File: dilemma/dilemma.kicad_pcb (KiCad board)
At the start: 2 copper layers, 134 x 106.9 mm, 84 parts, among them J1 S3B-PH-SM4-TB(LF)(SN), J2 Serial, J3 BATTERY_CONN_DEANS, J5 S3B-PH-SM4-TB(LF)(SN), SW1 SW_Push, SW10 SW_Push, SW11 SW_Push, SW12 SW_Push, SW13 SW_Push, SW14 SW_Push, SW15 SW_Push, SW16 SW_Push, SW17 locked, SW18 SW_Push, SW2 SW_Push, SW26 SW_SPST, SW3 SW_Push, SW37 SW_SPST, SW4 SW_Push, SW5 SW_Push, SW6 SW_Push, SW7 SW_Push, SW8 SW_Push, SW9 SW_Push, U2 eliteC

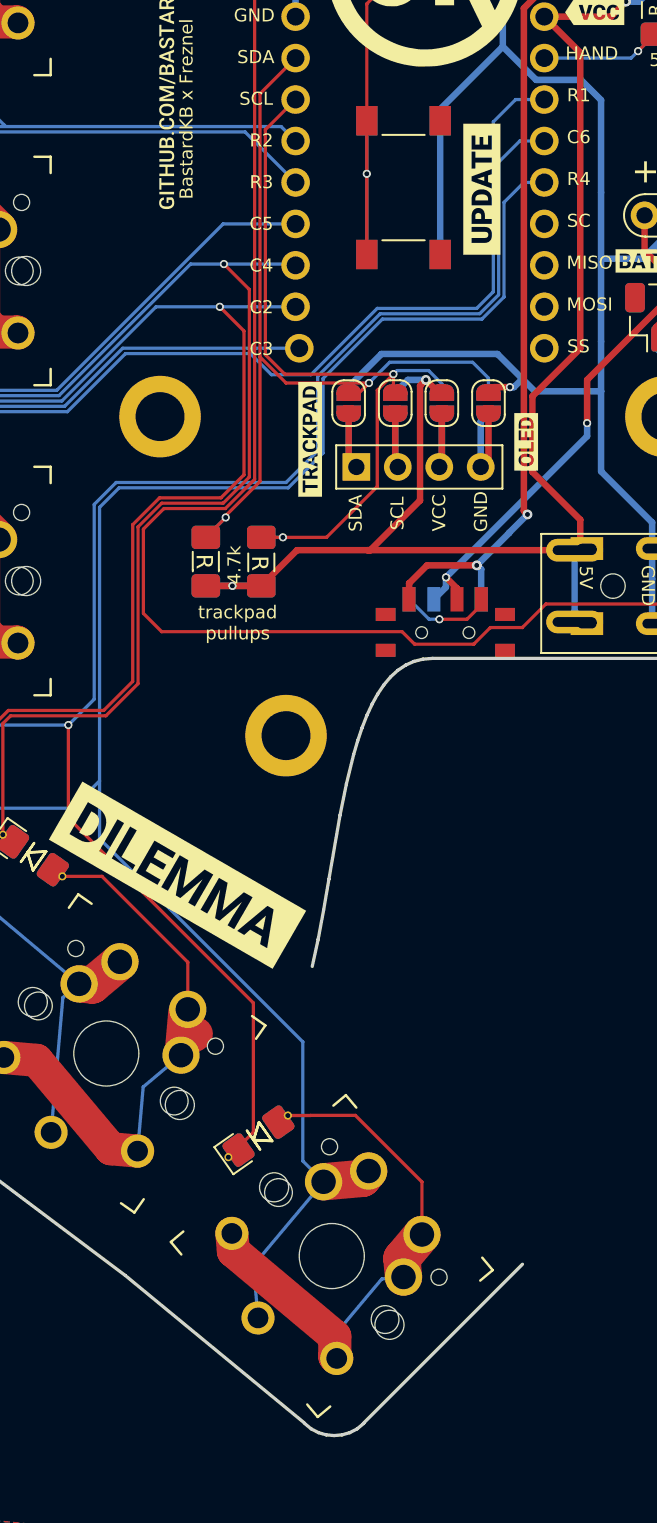
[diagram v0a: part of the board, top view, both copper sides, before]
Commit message: Create place for col6
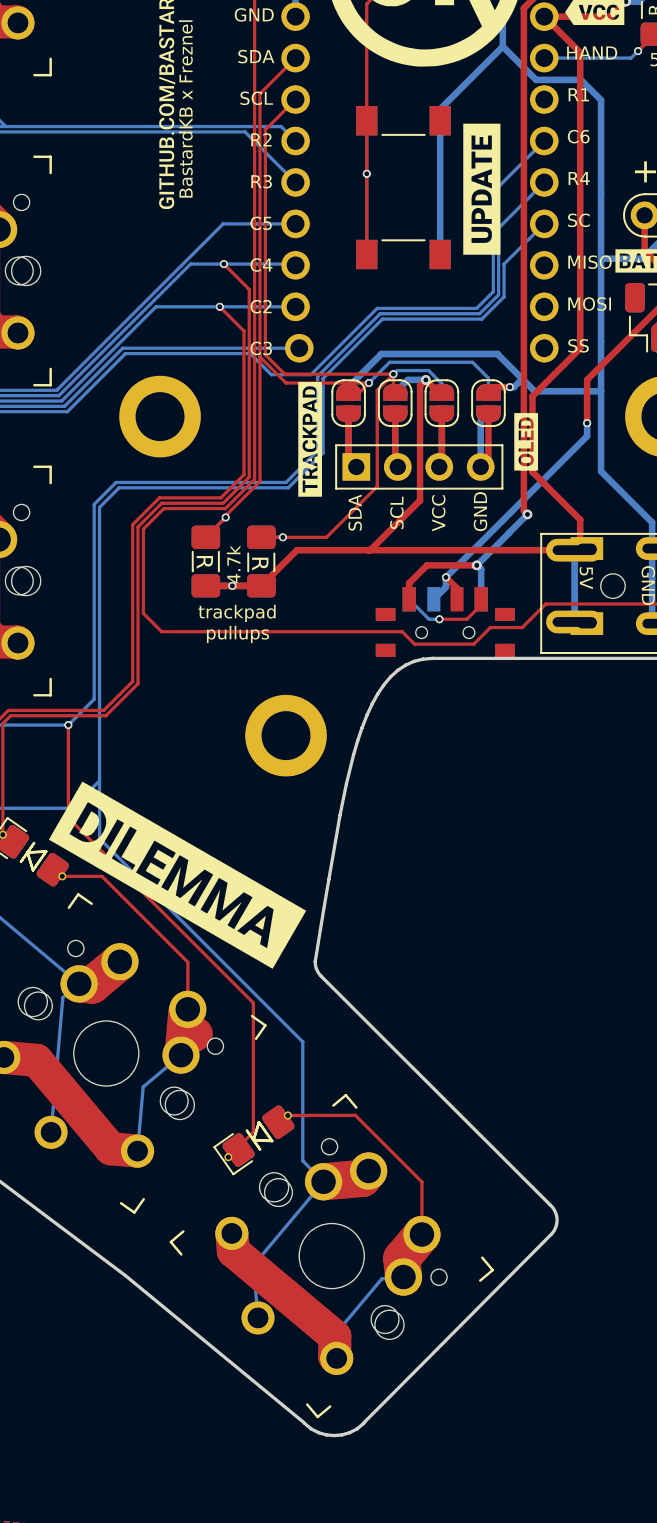
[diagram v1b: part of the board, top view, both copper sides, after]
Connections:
- U2 pad 15: miso_l -> sc_l
- U2 pad 16: sc_l -> row1_l
- U2 pad 17: row1_l -> col5_l
- U2 pad 18: col5_l -> row4_l
- U2 pad 19: row4_l -> miso_l
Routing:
- net row4_l: track 219.7 -> 216.2 mm
- net col5_l: track 154.8 -> 151.4 mm
- net row1_l: track 164.2 -> 160.9 mm
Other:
- outline, holes or cut-outs redrawn

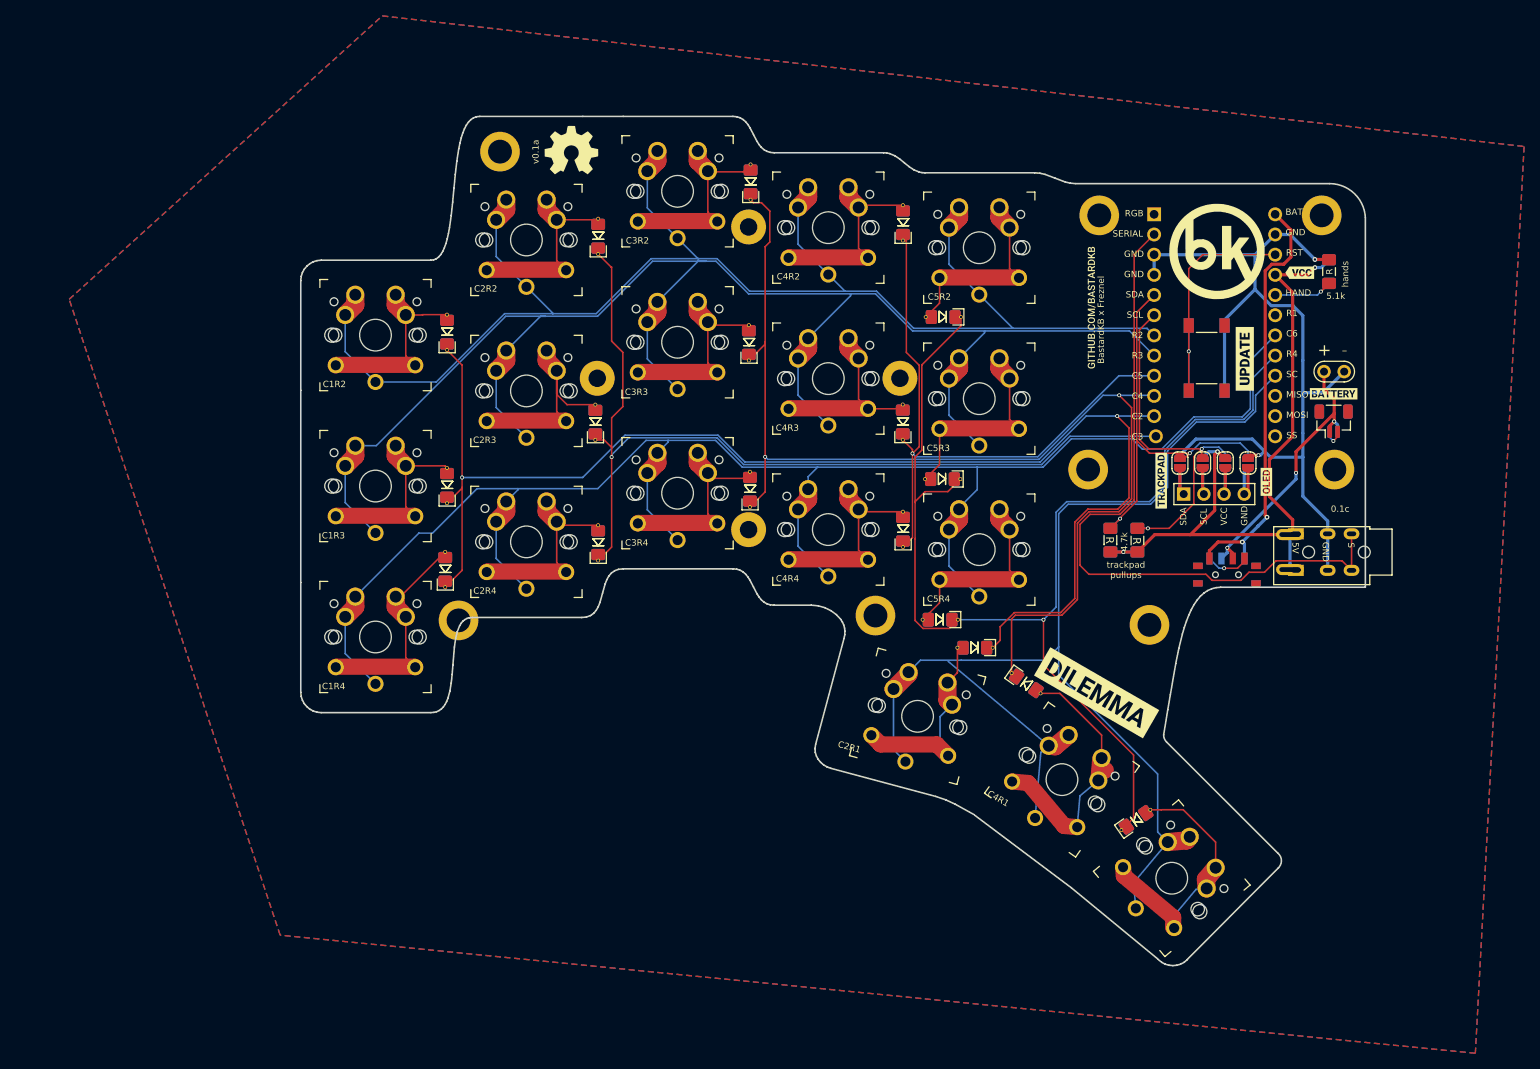
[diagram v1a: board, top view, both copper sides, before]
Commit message: Add 6th column
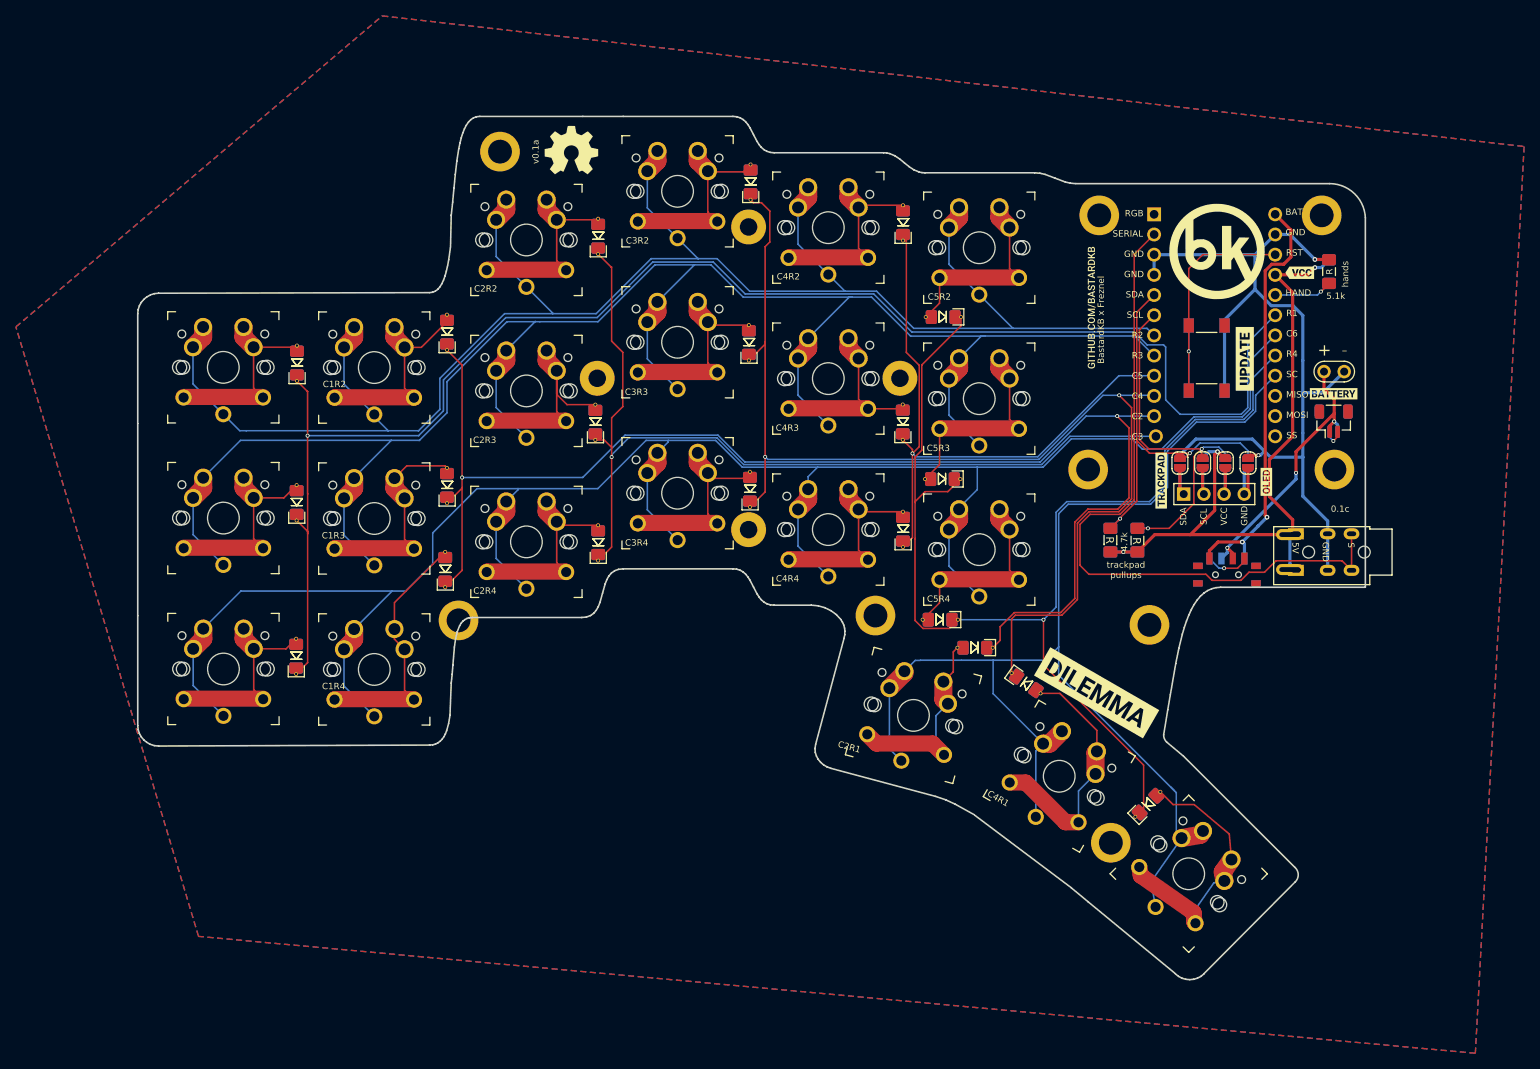
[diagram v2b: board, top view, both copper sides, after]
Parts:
- added D27: D, local-libraries:D_1206_handsolder_reversible, F.Cu at (105.5, 54.7)
- added D28: D, local-libraries:D_1206_handsolder_reversible, F.Cu at (105.5, 72.3)
- added D29: D, local-libraries:D_1206_handsolder_reversible, F.Cu at (105.4, 91.6)
- added REF**: MountingHole_3mm_Pad_thin, footprints:MountingHole_3mm_Pad_thin, F.Cu at (208.0, 115.1)
- added SW19: SW_Push, local-libraries:SW_MX_choc, F.Cu at (96.3, 55.2)
- added SW20: SW_Push, local-libraries:SW_MX_choc, F.Cu at (96.3, 74.2)
- added SW21: SW_Push, local-libraries:SW_MX_choc, F.Cu at (96.3, 93.2)
- moved SW1 4.09 mm to (115.3, 55.3)
- moved SW2 4.09 mm to (115.3, 74.3)
- moved SW3 4.09 mm to (115.3, 93.3)
- moved D34 2.48 mm to (212.7, 110.2), turned to 45 degrees
- moved SW18 2.21 mm to (217.8, 119.0), turned to -45 degrees
- moved SW17 0.55 mm to (201.5, 106.7), turned to -30 degrees
- moved SW16 0.53 mm to (183.1, 99.0)
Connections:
- U2 pad 19: miso_l -> col6_l
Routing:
- net col6_l: track 0.00 -> 195.3 mm, vias 0 -> 1
- net row4_l: track 216.2 -> 259.2 mm
- net row2_l: track 191.3 -> 232.1 mm
- net row3_l: track 208.1 -> 247.0 mm
- net Net-(SW20-Pad2): track 0.00 -> 26.0 mm
- net Net-(SW21-Pad2): track 0.00 -> 25.8 mm
- net Net-(SW19-Pad2): track 0.00 -> 25.4 mm
- net Net-(D5-Pad2): track 28.5 -> 32.9 mm
- net Net-(D3-Pad2): track 25.2 -> 27.5 mm
- net Net-(D4-Pad2): track 25.2 -> 27.3 mm
- net row1_l: track 160.9 -> 159.4 mm
- net col5_l: track 151.4 -> 150.1 mm
- net Net-(D33-Pad2): track 33.4 -> 32.3 mm
- net Net-(D34-Pad2): track 34.2 -> 34.9 mm
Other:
- board size 134 x 106.9 mm -> 154.5 x 108.7 mm
